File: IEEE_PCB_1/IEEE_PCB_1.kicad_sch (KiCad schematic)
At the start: 17 parts, among them U1 555, U2 4017, U3 EG1218, U4 CR2025TR

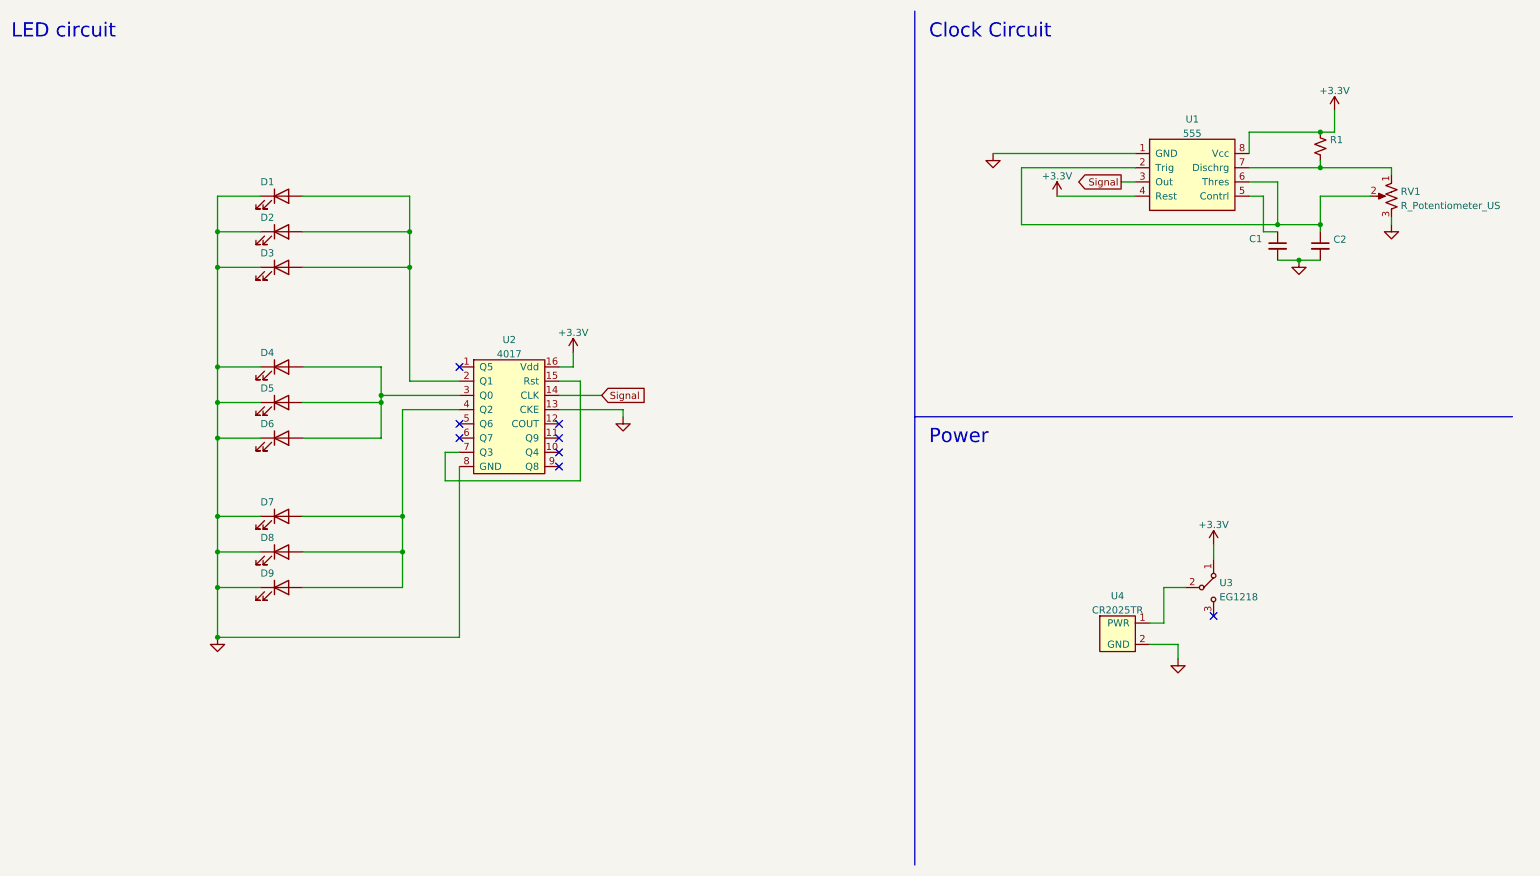
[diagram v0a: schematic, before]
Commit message: Rev 10/8/22
changed the logo footprint
changed the resistor footprint
added more vias to the power
altered traces to better fit the ESR standards
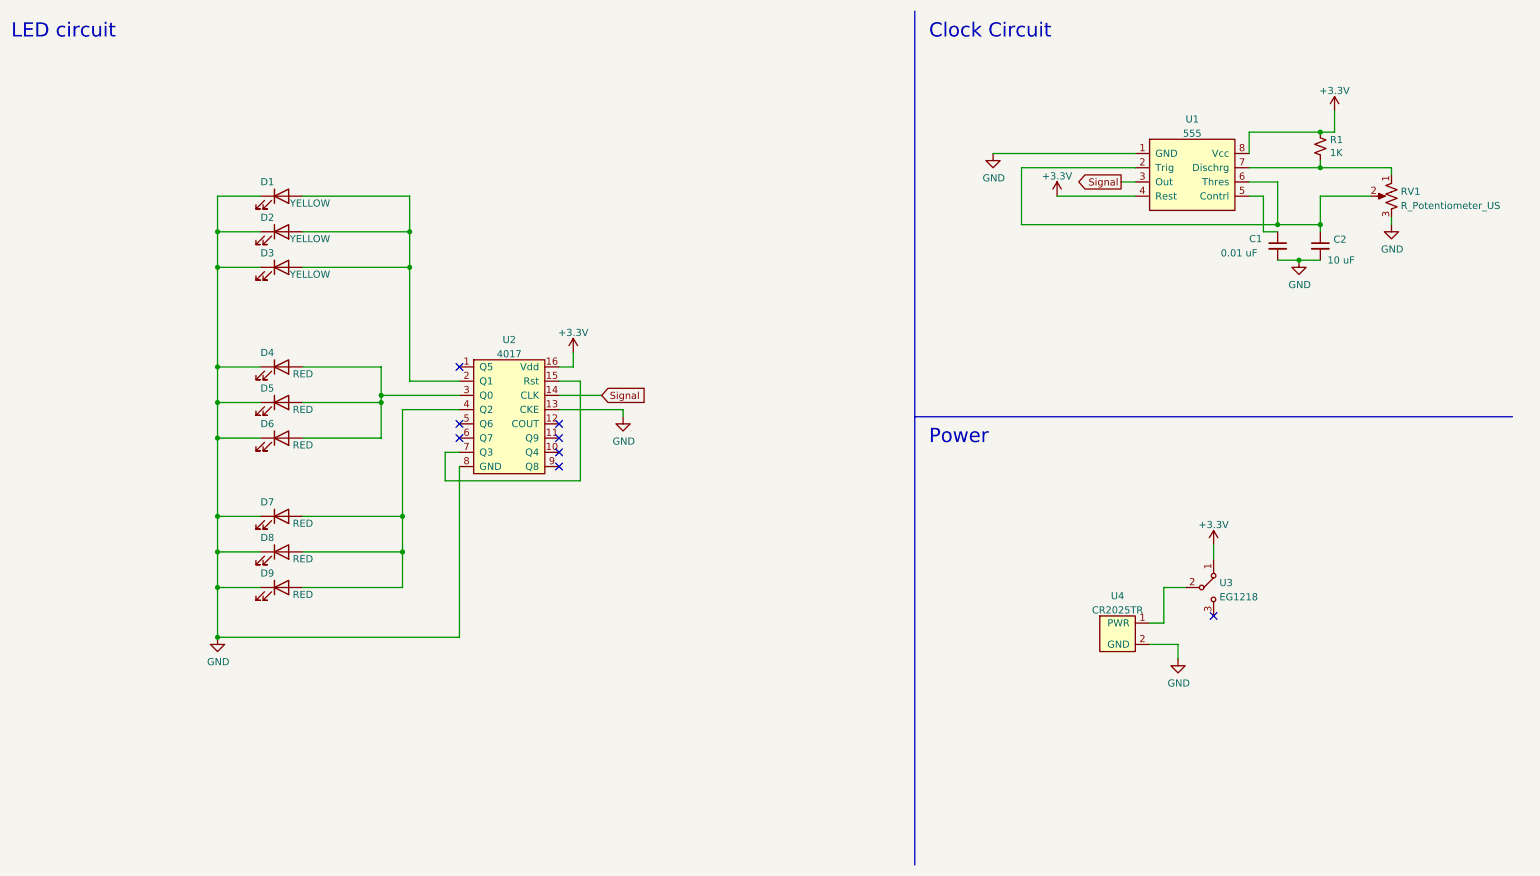
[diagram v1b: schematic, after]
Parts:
- C1: value (none) -> 0.01 uF; footprint (none) -> Capacitor_THT:CP_Radial_D5.0mm_P2.00mm
- C2: value (none) -> 10 uF; footprint (none) -> Capacitor_THT:CP_Radial_D5.0mm_P2.00mm
- D1, D2, D3: value (none) -> YELLOW; footprint (none) -> LED_THT:LED_D5.0mm_Clear
- D4, D5, D6, D7, D8, D9: value (none) -> RED; footprint (none) -> LED_THT:LED_D5.0mm_Clear
- R1: value (none) -> 1K; footprint (none) -> Resistor_THT:R_Axial_DIN0207_L6.3mm_D2.5mm_P7.62mm_Horizontal
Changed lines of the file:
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@@
       (effects (font (size 1.27 1.27)) (justify left))
     )
-    (property "Value" "" (id 1) (at 232.41 55.88 0)
-      (effects (font (size 1.27 1.27)) (justify left))
-    )
-    (property "Footprint" "" (id 2) (at 242.57 54.61 0)
+    (property "Value" "0.01 uF" (id 1) (at 232.41 55.88 0)
+      (effects (font (size 1.27 1.27)) (justify left))
+    )
+    (property "Footprint" "Capacitor_THT:CP_Radial_D5.0mm_P2.00mm" (id 2) (at 242.57 54.61 0)
       (effects (font (size 1.27 1.27)) hide)
     )
@@
       (effects (font (size 1.27 1.27)) (justify left))
     )
-    (property "Value" "" (id 1) (at 251.9172 37.973 0)
-      (effects (font (size 1.27 1.27)) (justify left))
-    )
-    (property "Footprint" "" (id 2) (at 250.19 36.83 0)
+    (property "Value" "1K" (id 1) (at 251.9172 37.973 0)
+      (effects (font (size 1.27 1.27)) (justify left))
+    )
+    (property "Footprint" "Resistor_THT:R_Axial_DIN0207_L6.3mm_D2.5mm_P7.62mm_Horizontal" (id 2) (at 250.19 36.83 0)
       (effects (font (size 1.27 1.27)) hide)
     )
@@
       (effects (font (size 1.27 1.27)) (justify left))
     )
-    (property "Value" "" (id 1) (at 251.46 57.15 0)
-      (effects (font (size 1.27 1.27)) (justify left))
-    )
-    (property "Footprint" "" (id 2) (at 250.19 54.61 0)
+    (property "Value" "10 uF" (id 1) (at 251.46 57.15 0)
+      (effects (font (size 1.27 1.27)) (justify left))
+    )
+    (property "Footprint" "Capacitor_THT:CP_Radial_D5.0mm_P2.00mm" (id 2) (at 250.19 54.61 0)
       (effects (font (size 1.27 1.27)) hide)
     )
@@
       (effects (font (size 1.27 1.27)) hide)
     )
-    (property "Value" "" (id 1) (at 246.507 61.5442 0))
+    (property "Value" "GND" (id 1) (at 246.507 61.5442 0))
     (property "Footprint" "" (id 2) (at 246.38 57.15 0)
       (effects (font (size 1.27 1.27)) hide)
@@
       (effects (font (size 1.27 1.27)) hide)
     )
-    (property "Value" "" (id 1) (at 191.897 42.4942 0))
+    (property "Value" "GND" (id 1) (at 191.897 42.4942 0))
     (property "Footprint" "" (id 2) (at 191.77 38.1 0)
       (effects (font (size 1.27 1.27)) hide)
@@
       (effects (font (size 1.27 1.27)) hide)
     )
-    (property "Value" "" (id 1) (at 125.857 89.4842 0))
+    (property "Value" "GND" (id 1) (at 125.857 89.4842 0))
     (property "Footprint" "" (id 2) (at 125.73 85.09 0)
       (effects (font (size 1.27 1.27)) hide)
@@
       (effects (font (size 1.27 1.27)) hide)
     )
-    (property "Value" "" (id 1) (at 263.017 55.1942 0))
+    (property "Value" "GND" (id 1) (at 263.017 55.1942 0))
     (property "Footprint" "" (id 2) (at 262.89 50.8 0)
       (effects (font (size 1.27 1.27)) hide)
@@
       (effects (font (size 1.27 1.27)) hide)
     )
-    (property "Value" "" (id 1) (at 224.917 132.6642 0))
+    (property "Value" "GND" (id 1) (at 224.917 132.6642 0))
     (property "Footprint" "" (id 2) (at 224.79 128.27 0)
       (effects (font (size 1.27 1.27)) hide)
@@
     (in_bom yes) (on_board yes)
     (property "Reference" "D1" (id 0) (at 62.23 43.18 0))
-    (property "Value" "" (id 1) (at 69.85 46.99 0))
-    (property "Footprint" "" (id 2) (at 64.77 45.72 0)
+    (property "Value" "YELLOW" (id 1) (at 69.85 46.99 0))
+    (property "Footprint" "LED_THT:LED_D5.0mm_Clear" (id 2) (at 64.77 45.72 0)
       (effects (font (size 1.27 1.27)) hide)
     )
@@
     (in_bom yes) (on_board yes)
     (property "Reference" "D2" (id 0) (at 62.23 49.53 0))
-    (property "Value" "" (id 1) (at 69.85 53.34 0))
-    (property "Footprint" "" (id 2) (at 64.77 52.07 0)
+    (property "Value" "YELLOW" (id 1) (at 69.85 53.34 0))
+    (property "Footprint" "LED_THT:LED_D5.0mm_Clear" (id 2) (at 64.77 52.07 0)
       (effects (font (size 1.27 1.27)) hide)
     )
@@
     (in_bom yes) (on_board yes)
     (property "Reference" "D3" (id 0) (at 62.23 55.88 0))
-    (property "Value" "" (id 1) (at 69.85 59.69 0))
-    (property "Footprint" "" (id 2) (at 64.77 58.42 0)
+    (property "Value" "YELLOW" (id 1) (at 69.85 59.69 0))
+    (property "Footprint" "LED_THT:LED_D5.0mm_Clear" (id 2) (at 64.77 58.42 0)
       (effects (font (size 1.27 1.27)) hide)
     )
@@
     (in_bom yes) (on_board yes)
     (property "Reference" "D4" (id 0) (at 62.23 73.66 0))
-    (property "Value" "" (id 1) (at 68.58 77.47 0))
-    (property "Footprint" "" (id 2) (at 64.77 76.2 0)
+    (property "Value" "RED" (id 1) (at 68.58 77.47 0))
+    (property "Footprint" "LED_THT:LED_D5.0mm_Clear" (id 2) (at 64.77 76.2 0)
       (effects (font (size 1.27 1.27)) hide)
     )
@@
     (in_bom yes) (on_board yes)
     (property "Reference" "D5" (id 0) (at 62.23 80.01 0))
-    (property "Value" "" (id 1) (at 68.58 83.82 0))
-    (property "Footprint" "" (id 2) (at 64.77 82.55 0)
+    (property "Value" "RED" (id 1) (at 68.58 83.82 0))
+    (property "Footprint" "LED_THT:LED_D5.0mm_Clear" (id 2) (at 64.77 82.55 0)
       (effects (font (size 1.27 1.27)) hide)
     )
@@
     (in_bom yes) (on_board yes)
     (property "Reference" "D6" (id 0) (at 62.23 86.36 0))
-    (property "Value" "" (id 1) (at 68.58 90.17 0))
-    (property "Footprint" "" (id 2) (at 64.77 88.9 0)
+    (property "Value" "RED" (id 1) (at 68.58 90.17 0))
+    (property "Footprint" "LED_THT:LED_D5.0mm_Clear" (id 2) (at 64.77 88.9 0)
       (effects (font (size 1.27 1.27)) hide)
     )
@@
     (in_bom yes) (on_board yes)
     (property "Reference" "D7" (id 0) (at 62.23 100.33 0))
-    (property "Value" "" (id 1) (at 68.58 104.14 0))
-    (property "Footprint" "" (id 2) (at 64.77 102.87 0)
+    (property "Value" "RED" (id 1) (at 68.58 104.14 0))
+    (property "Footprint" "LED_THT:LED_D5.0mm_Clear" (id 2) (at 64.77 102.87 0)
       (effects (font (size 1.27 1.27)) hide)
     )
@@
     (in_bom yes) (on_board yes)
     (property "Reference" "D8" (id 0) (at 62.23 106.68 0))
-    (property "Value" "" (id 1) (at 68.58 110.49 0))
-    (property "Footprint" "" (id 2) (at 64.77 109.22 0)
+    (property "Value" "RED" (id 1) (at 68.58 110.49 0))
+    (property "Footprint" "LED_THT:LED_D5.0mm_Clear" (id 2) (at 64.77 109.22 0)
       (effects (font (size 1.27 1.27)) hide)
     )
@@
     (in_bom yes) (on_board yes)
     (property "Reference" "D9" (id 0) (at 62.23 113.03 0))
-    (property "Value" "" (id 1) (at 68.58 116.84 0))
-    (property "Footprint" "" (id 2) (at 64.77 115.57 0)
+    (property "Value" "RED" (id 1) (at 68.58 116.84 0))
+    (property "Footprint" "LED_THT:LED_D5.0mm_Clear" (id 2) (at 64.77 115.57 0)
       (effects (font (size 1.27 1.27)) hide)
     )
@@
       (effects (font (size 1.27 1.27)) hide)
     )
-    (property "Value" "" (id 1) (at 53.467 128.8542 0))
+    (property "Value" "GND" (id 1) (at 53.467 128.8542 0))
     (property "Footprint" "" (id 2) (at 53.34 124.46 0)
       (effects (font (size 1.27 1.27)) hide)
@@
     )
     (path "/00000000-0000-0000-0000-000062de663b"
-      (reference "R1") (unit 1) (value "1K") (footprint "Resistor_THT:R_Axial_DIN0309_L9.0mm_D3.2mm_P12.70mm_Horizontal")
+      (reference "R1") (unit 1) (value "1K") (footprint "Resistor_THT:R_Axial_DIN0207_L6.3mm_D2.5mm_P7.62mm_Horizontal")
     )
     (path "/dcf2420a-03f3-49a4-a2ed-40e1d2acfce4"

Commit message: rev - Matthew
editted the ball ornament
added resistors
fixed any battery and switch symbols
fixed any acid traps
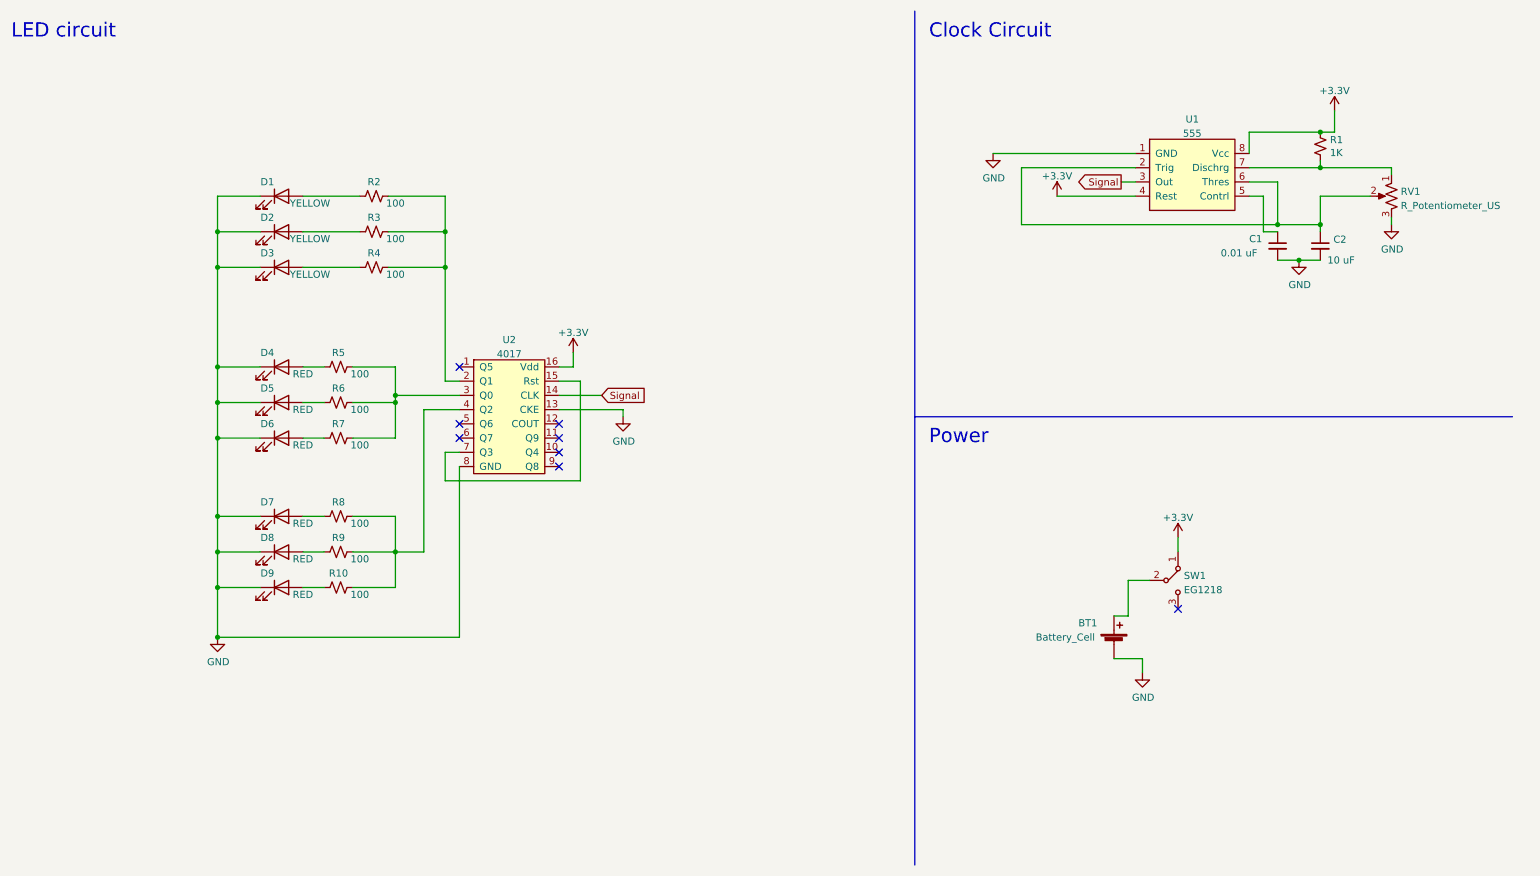
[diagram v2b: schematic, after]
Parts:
- removed U4: CR2025TR, IEEE_Ornament:CR2025TR, symbol IEEE_Ornament:CR2025TR
- added BT1: Battery_Cell, IEEE_Ornament:CR2025TR, symbol Device:Battery_Cell
- added R10, R2, R3, R4, R5, R6, R7, R8, R9: 100, Resistor_SMD:R_0603_1608Metric_Pad0.98x0.95mm_HandSolder, symbol Device:R_Small_US
- renumbered U3 to SW1
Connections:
- net GND: now also BT1.2 (-)
- net at SW1.2: now also BT1.1 (+)
- new net: D1.2 (A), R2.1
- new net: D2.2 (A), R3.1
- new net: D3.2 (A), R4.1
- new net: D4.2 (A), R5.1
- new net: D5.2 (A), R6.1
- new net: D6.2 (A), R7.1
- new net: D7.2 (A), R8.1
- new net: D8.2 (A), R9.1
- new net: D9.2 (A), R10.1
- new net: R10.2, R8.2, R9.2, U2.4 (Q2)
- new net: R5.2, R6.2, R7.2, U2.3 (Q0)
- new net: R2.2, R3.2, R4.2, U2.2 (Q1)
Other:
- moved on the sheet: SW1
